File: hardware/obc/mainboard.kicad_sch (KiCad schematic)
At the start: 0 parts

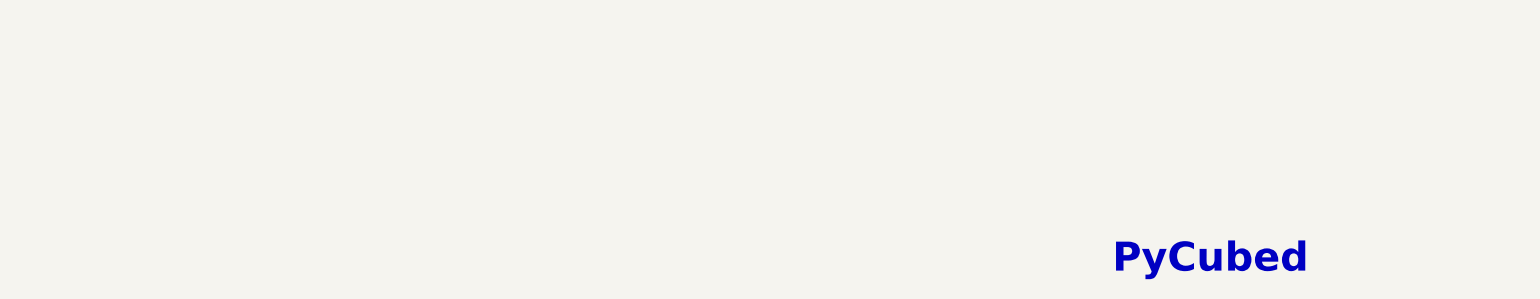
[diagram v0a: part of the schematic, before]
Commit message: OBC: Continuing work towards the next revision
- Changed 3.3V names on Avionics page
- Removed buss protection-bypass jumpers
- Edited SPI buss protection
- Removed U302
- Removed JP401
- Other label/clean up modifications
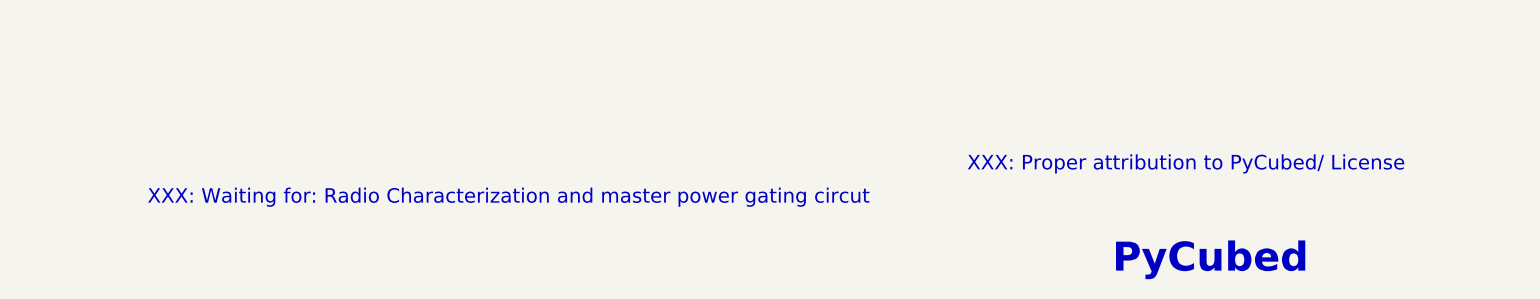
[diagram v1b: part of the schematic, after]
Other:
- note added: "XXX: Proper attribution to PyCubed/ License"
- note added: "XXX: Waiting for: Radio Characterization and master power gating circut"
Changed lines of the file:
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@@
 		(comment 1 "Derived from PyCubed Mainboard v5")
+	)
+	(text "XXX: Proper attribution to PyCubed/ License"
+		(exclude_from_sim no)
+		(at 206.756 163.322 0)
+		(effects
+			(font
+				(size 2.54 2.54)
+			)
+		)
 	)
 	(text "GND is ground reference for components on the schematic. \nGNDREF is the negative terminal of the battery board."
@@
 			)
 		)
+	)
+	(text "XXX: Waiting for: Radio Characterization and master power gating circut\n"
+		(exclude_from_sim no)
+		(at 87.884 169.164 0)
+		(effects
+			(font
+				(size 2.54 2.54)
+			)
+		)

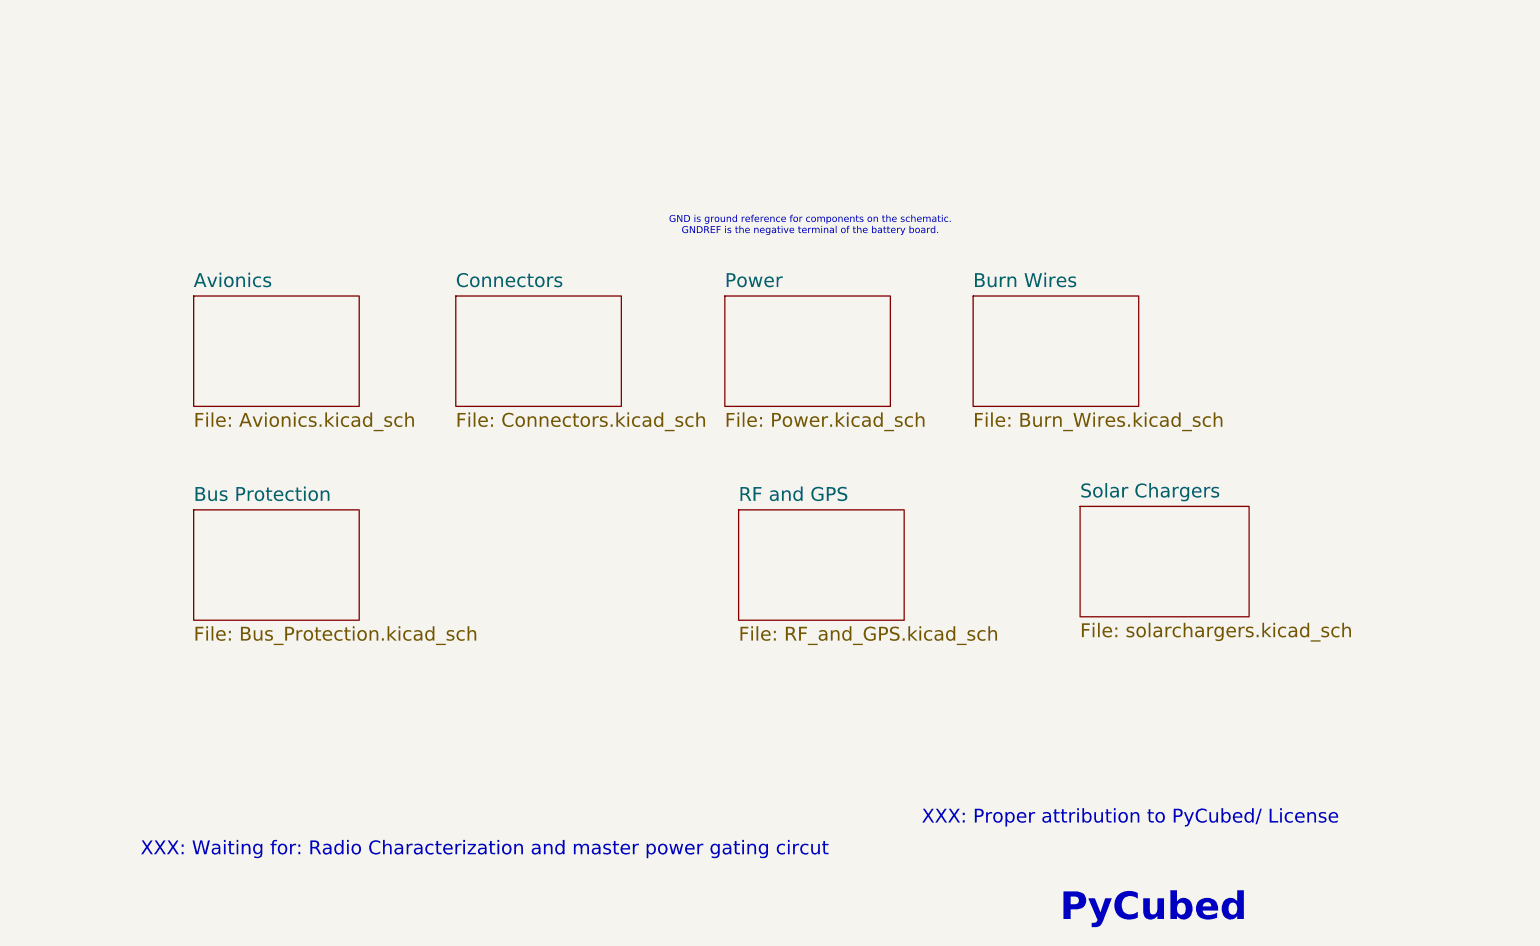
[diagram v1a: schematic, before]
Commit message: obc: Attribution on first page
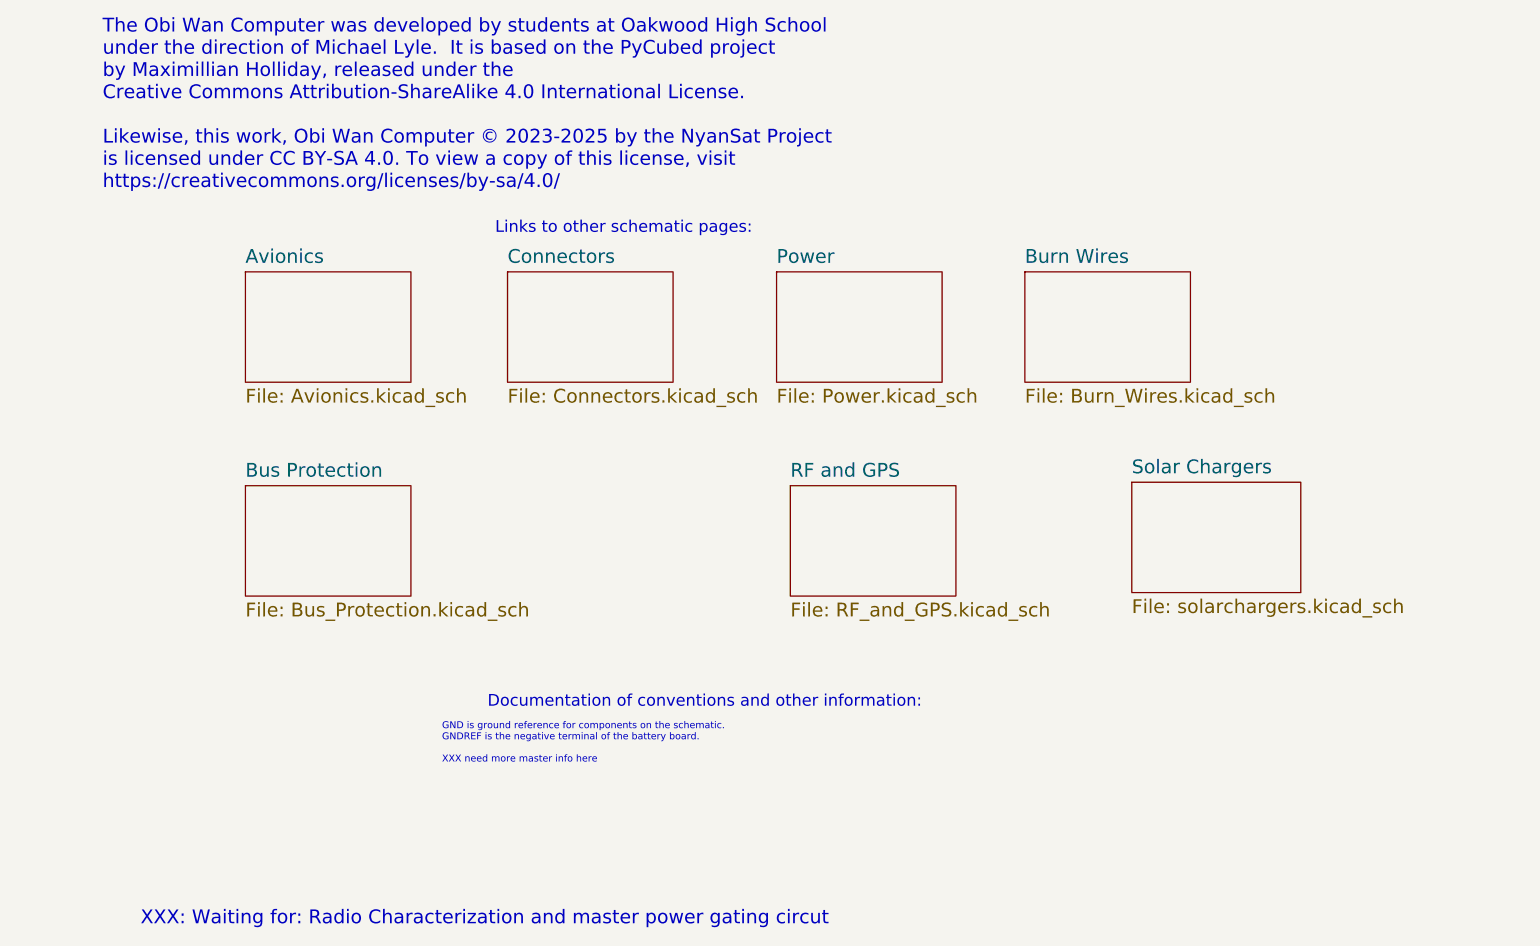
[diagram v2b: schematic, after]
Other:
- note added: "Documentation of conventions and other information:"
- note added: "GND is ground reference for components on the schematic. GNDREF is the negative terminal of the battery board. XXX need more master info here"
- note added: "Links to other schematic pages:"
- note added: "The Obi Wan Computer was developed by students at Oakwood High School under the direction of Michael Lyle. It is based on the PyCubed project by Maximillian Holliday, released under the Creative Commons Attribution-ShareAlike 4.0 International License. Likewise, this work, Obi Wan Computer © 2023-2025 by the NyanSat Project is licensed under CC BY-SA 4.0. To view a copy of this license, visit htt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"
- note removed: "GND is ground reference for components on the schematic. GNDREF is the negative terminal of the battery board."
- note removed: "PyCubed"
- note removed: "XXX: Proper attribution to PyCubed/ License"
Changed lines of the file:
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@@
 		(comment 1 "Derived from PyCubed Mainboard v5")
 	)
-	(text "XXX: Proper attribution to PyCubed/ License"
-		(exclude_from_sim no)
-		(at 206.756 163.322 0)
+	(text "The Obi Wan Computer was developed by students at Oakwood High School\nunder the direction of Michael Lyle.  It is based on the PyCubed project\nby Maximillian Holliday, released under the\nCreative Commons Attribution-ShareAlike 4.0 International License.\n\nLikewise, this work, Obi Wan Computer © 2023-2025 by the NyanSat Project\nis licensed under CC BY-SA 4.0. To view a copy of this license, visit \nhttps://creativecommons.org/licenses/by-sa/4.0/"
+		(exclude_from_sim no)
+		(at 17.526 32.004 0)
 		(effects
 			(font
 				(size 2.54 2.54)
 			)
-		)
-	)
-	(text "GND is ground reference for components on the schematic. \nGNDREF is the negative terminal of the battery board."
-		(exclude_from_sim no)
-		(at 147.828 54.356 0)
+			(justify left)
+			(href "https://creativecommons.org/licenses/by-sa/4.0/")
+		)
+	)
+	(text "GND is ground reference for components on the schematic. \nGNDREF is the negative terminal of the battery board.\n\nXXX need more master info here"
+		(exclude_from_sim no)
+		(at 80.01 149.606 0)
 		(effects
 			(font
 				(size 1.27 1.27)
 			)
+			(justify left)
 		)
 	)
 	(text "XXX: Waiting for: Radio Characterization and master power gating circut\n"
 		(exclude_from_sim no)
-		(at 87.884 169.164 0)
+		(at 87.884 181.864 0)
 		(effects
 			(font
@@
 		)
 	)
-	(text "PyCubed"
-		(exclude_from_sim no)
-		(at 193.802 182.88 0)
-		(effects
-			(font
-				(size 5.08 5.08)
-				(thickness 1.016)
-				(bold yes)
+	(text "Links to other schematic pages:"
+		(exclude_from_sim no)
+		(at 89.789 56.007 0)
+		(effects
+			(font
+				(size 2.159 2.159)
 			)
 			(justify left bottom)
 		)
 	)
-	(sheet
-		(at 34.29 67.31)
+	(text "Documentation of conventions and other information:"
+		(exclude_from_sim no)
+		(at 88.392 143.256 0)
+		(effects
+			(font
+				(size 2.159 2.159)
+			)
+			(justify left bottom)
+		)
+	)
+	(sheet
+		(at 43.815 62.865)
 		(size 30.48 20.32)
 		(fields_autoplaced yes)
@@
 		)
 		(property "Sheetname" "Avionics"
-			(at 34.29 65.9634 0)
+			(at 43.815 61.5184 0)
 			(effects
 				(font
@@
 		)
 		(property "Sheetfile" "Avionics.kicad_sch"
-			(at 34.29 88.7226 0)
+			(at 43.815 84.2776 0)
 			(effects
 				(font
@@
 	)
 	(sheet
-		(at 132.08 67.31)
+		(at 141.605 62.865)
 		(size 30.48 20.32)
 		(fields_autoplaced yes)
@@
 		)
 		(property "Sheetname" "Power"
-			(at 132.08 65.9634 0)
+			(at 141.605 61.5184 0)
 			(effects
 				(font
@@
 		)
 		(property "Sheetfile" "Power.kicad_sch"
-			(at 132.08 88.7226 0)
+			(at 141.605 84.2776 0)
 			(effects
 				(font
@@
 	)
 	(sheet
-		(at 82.55 67.31)
+		(at 92.075 62.865)
 		(size 30.48 20.32)
 		(fields_autoplaced yes)
@@
 		)
 		(property "Sheetname" "Connectors"
-			(at 82.55 65.9634 0)
+			(at 92.075 61.5184 0)
 			(effects
 				(font
@@
 		)
 		(property "Sheetfile" "Connectors.kicad_sch"
-			(at 82.55 88.7226 0)
+			(at 92.075 84.2776 0)
 			(effects
 				(font
@@
 	)
 	(sheet
-		(at 134.62 106.68)
+		(at 144.145 102.235)
 		(size 30.48 20.32)
 		(fields_autoplaced yes)
@@
 		)
 		(property "Sheetname" "RF and GPS"
-			(at 134.62 105.3334 0)
+			(at 144.145 100.8884 0)
 			(effects
 				(font
@@
 		)
 		(property "Sheetfile" "RF_and_GPS.kicad_sch"
-			(at 134.62 128.0926 0)
+			(at 144.145 123.6476 0)
 			(effects
 				(font
@@
 	)
 	(sheet
-		(at 177.8 67.31)
+		(at 187.325 62.865)
 		(size 30.48 20.32)
 		(fields_autoplaced yes)
@@
 		)
 		(property "Sheetname" "Burn Wires"
-			(at 177.8 65.9634 0)
+			(at 187.325 61.5184 0)
 			(effects
 				(font
@@
 		)
 		(property "Sheetfile" "Burn_Wires.kicad_sch"
-			(at 177.8 88.7226 0)
+			(at 187.325 84.2776 0)
 			(effects
 				(font
@@
 	)
 	(sheet
-		(at 34.29 106.68)
+		(at 43.815 102.235)
 		(size 30.48 20.32)
 		(fields_autoplaced yes)
@@
 		)
 		(property "Sheetname" "Bus Protection"
-			(at 34.29 105.3334 0)
+			(at 43.815 100.8884 0)
 			(effects
 				(font
@@
 		)
 		(property "Sheetfile" "Bus_Protection.kicad_sch"
-			(at 34.29 128.0926 0)
+			(at 43.815 123.6476 0)
 			(effects
 				(font
@@
 	)
 	(sheet
-		(at 197.485 106.045)
+		(at 207.01 101.6)
 		(size 31.115 20.32)
 		(fields_autoplaced yes)
@@
 		)
 		(property "Sheetname" "Solar Chargers"
-			(at 197.485 104.6984 0)
+			(at 207.01 100.2534 0)
 			(effects
 				(font
@@
 		)
 		(property "Sheetfile" "solarchargers.kicad_sch"
-			(at 197.485 127.4576 0)
-			(effects
-				(font
+			(at 207.01 123.0126 0)
+			(effects
+				(font

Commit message: OBC: Added new power supervisor and watch dog circuit
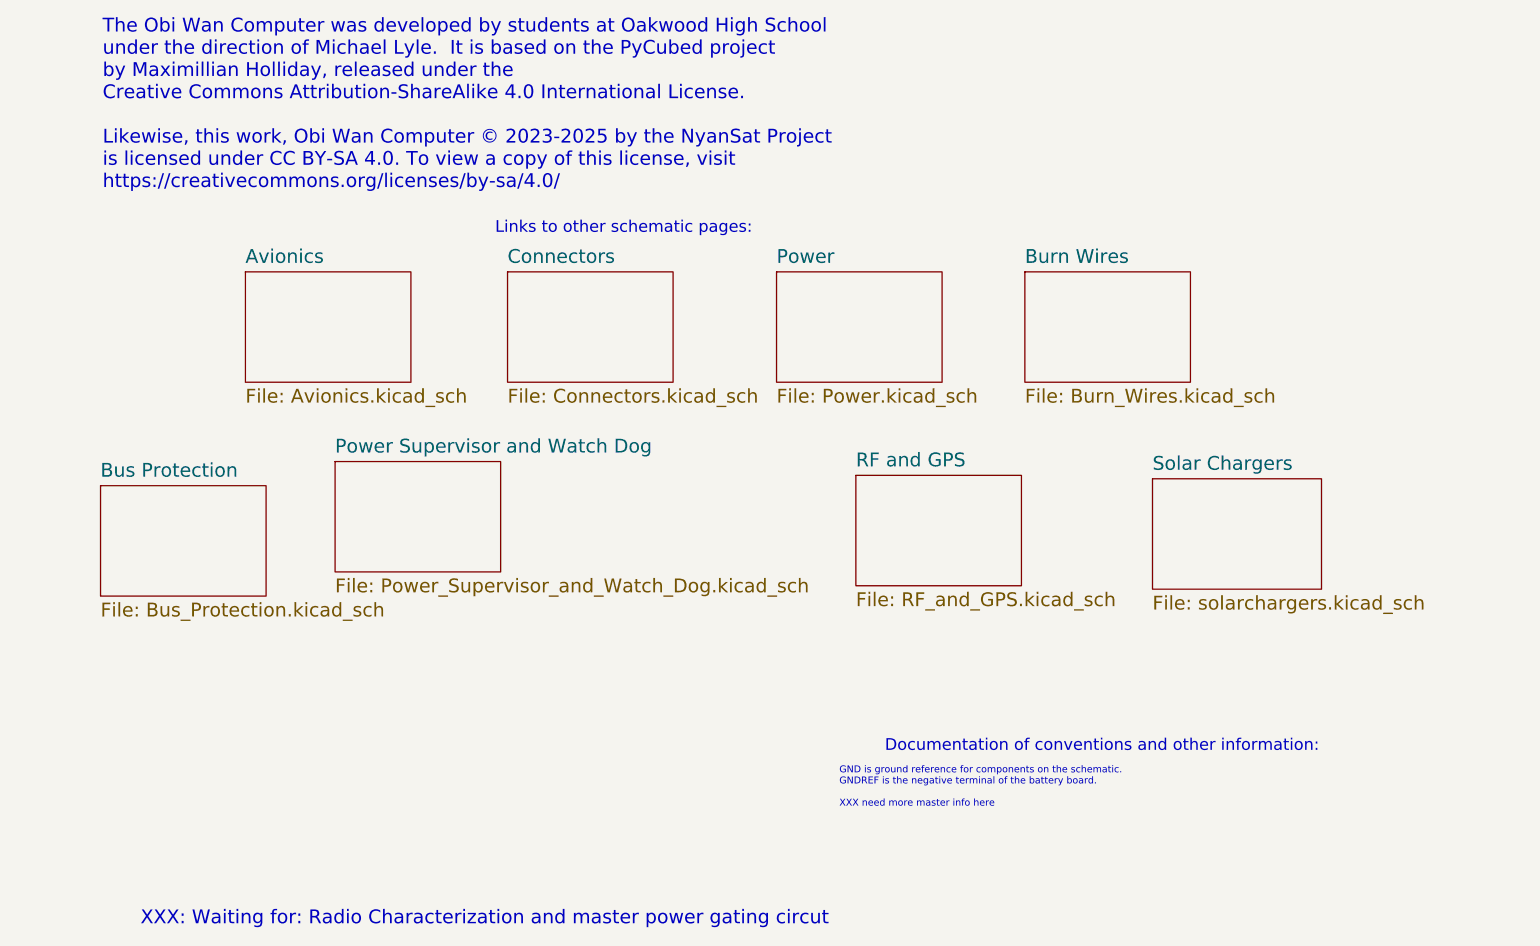
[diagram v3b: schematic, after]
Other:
- added sheet Power Supervisor and Watch Dog (Power_Supervisor_and_Watch_Dog.kicad_sch)
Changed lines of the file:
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@@
 	(text "GND is ground reference for components on the schematic. \nGNDREF is the negative terminal of the battery board.\n\nXXX need more master info here"
 		(exclude_from_sim no)
-		(at 80.01 149.606 0)
+		(at 153.162 157.734 0)
 		(effects
 			(font
@@
 	(text "Documentation of conventions and other information:"
 		(exclude_from_sim no)
-		(at 88.392 143.256 0)
+		(at 161.544 151.384 0)
 		(effects
 			(font
@@
 	)
 	(sheet
-		(at 144.145 102.235)
+		(at 156.21 100.33)
 		(size 30.48 20.32)
 		(fields_autoplaced yes)
@@
 		)
 		(property "Sheetname" "RF and GPS"
-			(at 144.145 100.8884 0)
+			(at 156.21 98.9834 0)
 			(effects
 				(font
@@
 		)
 		(property "Sheetfile" "RF_and_GPS.kicad_sch"
-			(at 144.145 123.6476 0)
+			(at 156.21 121.7426 0)
 			(effects
 				(font
@@
 	)
 	(sheet
-		(at 43.815 102.235)
+		(at 17.145 102.235)
 		(size 30.48 20.32)
 		(fields_autoplaced yes)
@@
 		)
 		(property "Sheetname" "Bus Protection"
-			(at 43.815 100.8884 0)
+			(at 17.145 100.8884 0)
 			(effects
 				(font
@@
 		)
 		(property "Sheetfile" "Bus_Protection.kicad_sch"
-			(at 43.815 123.6476 0)
+			(at 17.145 123.6476 0)
 			(effects
 				(font
@@
 	)
 	(sheet
-		(at 207.01 101.6)
+		(at 60.325 97.79)
+		(size 30.48 20.32)
+		(fields_autoplaced yes)
+		(stroke
+			(width 0)
+			(type solid)
+		)
+		(fill
+			(color 0 0 0 0.0000)
+		)
+		(property "Sheetname" "Power Supervisor and Watch Dog"
+			(at 60.325 96.4434 0)
+			(effects
+				(font
+					(size 2.54 2.54)
+				)
+				(justify left bottom)
+			)
+		)
+		(property "Sheetfile" "Power_Supervisor_and_Watch_Dog.kicad_sch"
+			(at 60.325 119.2026 0)
+			(effects
+				(font
+					(size 2.54 2.54)
+				)
+				(justify left top)
+			)
+		)
+		(instances
+			(project "mainboard"
+				(path "/e3ac22ea-6806-4807-a025-571315789c25"
+					(page "9")
+				)
+			)
+		)
+	)
+	(sheet
+		(at 210.82 100.965)
 		(size 31.115 20.32)
 		(fields_autoplaced yes)
@@
 		)
 		(property "Sheetname" "Solar Chargers"
-			(at 207.01 100.2534 0)
+			(at 210.82 99.6184 0)
 			(effects
 				(font
@@
 		)
 		(property "Sheetfile" "solarchargers.kicad_sch"
-			(at 207.01 123.0126 0)
-			(effects
-				(font
+			(at 210.82 122.3776 0)
+			(effects
+				(font
